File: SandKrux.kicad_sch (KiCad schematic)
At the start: 101 parts, among them CN1 527450697, J1 Conn_01x02, Q1 S8050, Q2 SI2301CDS-T1-GE3, U1 K210_C913414, U2 AXP173, U3 MT9700-N, U4 XC6206P182MR_C347373, U5 GD25LQ128EWIGR, U6 TMI7003C, U7 SGM803-TXN3/TR_C5152602, U8 XC6206P302MR_C347375, X1 X322526MMB4SI

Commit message: TFT CARD
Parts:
- added C51: 10uF, Capacitor_SMD:C_0201_0603Metric, symbol Device:C
- added R28, R29: 10K, Resistor_SMD:R_0201_0603Metric, symbol Device:R
- added U9: HX TF-CARD XG8P H1.5, easyeda2kicad:TF-SMD_HX-TF-CARD-XG8P-H1.5, symbol easyeda2kicad:HXTF-CARDXG8PH1.5
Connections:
- net GND: now also C51.1, U9.10 (GND), U9.11 (GND), U9.12 (GND), U9.6 (VSS2), U9.9 (GND)
- net at C37.1, C4.2, C49.1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: now also C51.2, R28.2, R29.2, U9.4 (VDD)
- new net: R29.1, U9.7 (DAT0)
- new net SPI1_CS_TF: U9.2 (CD/DAT3)
- new net SPI1_MISO: U9.5 (CLK)
- new net SPI1_MOSI: R28.1, U9.3 (CMD)
- no-connect marks 70 -> 72
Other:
- note added: "TF CARD"

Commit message: usb ports
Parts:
- added R30, R31: 5.1K, Resistor_SMD:R_0201_0603Metric, symbol Device:R
- added R32, R33, R34, R35, R36, R37, R38, R39: 1.5K, Resistor_SMD:R_0201_0603Metric, symbol Device:R
- added R40: NC, Resistor_SMD:R_0201_0603Metric, symbol Device:R
- added R41: 0R, Resistor_SMD:R_0201_0603Metric, symbol Device:R
- added SW1, SW2, SW3, SW4, SW5: TL3330AF130QG, easyeda2kicad:SW-SMD_E-SWITCH_TL3330, symbol easyeda2kicad:TL3330AF130QG
- added USB1: HYCW412-USBC16-065B, easyeda2kicad:USB-C-SMD_HYCW412-USBC16-065B, symbol easyeda2kicad:HYCW412-USBC16-065B
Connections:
- net GND: now also R30.1, R31.1, R41.2, SW2.2, SW2.3, SW2.4, SW3.2, SW3.3, SW3.4, SW4.2, SW4.3, SW4.4, SW5.3, SW5.4, USB1.13, USB1.14, USB1.15, USB1.16, USB1.A1B12 (GND), USB1.B1A12 (GND)
- net I2C_SCL: now also R37.2
- net I2C_SDA: now also R36.2
- net RST: now also SW1.1
- net at C37.1, C4.2, C49.1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: now also R32.2, R33.2, R34.2, R35.2, R36.1, R37.1, R38.1, R39.1, R40.2
- new net: R40.1, R41.1, SW5.2
- new net: SW1.3, SW1.4
- new net 5V_USB: USB1.A4B9 (VBUS), USB1.B4A9 (VBUS)
- new net CC1_2: R30.2, USB1.A5 (CC1)
- new net CC2_2: R31.2, USB1.B5 (CC2)
- new net IO17: R34.1
- new net IO19: R35.1
- new net KEY1: R38.2, SW3.1
- new net KEY2: R39.2, SW4.1
- new net KEY3: SW5.1
- new net PWRON: SW2.1
- new net U2RX: R33.1
- new net U2TX: R32.1
- new net USB_D+: USB1.A6 (DP1), USB1.B6 (DP2)
- new net USB_D-: USB1.A7 (DN1), USB1.B7 (DN2)
- no-connect marks 72 -> 74
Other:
- note added: "USB PORTS"

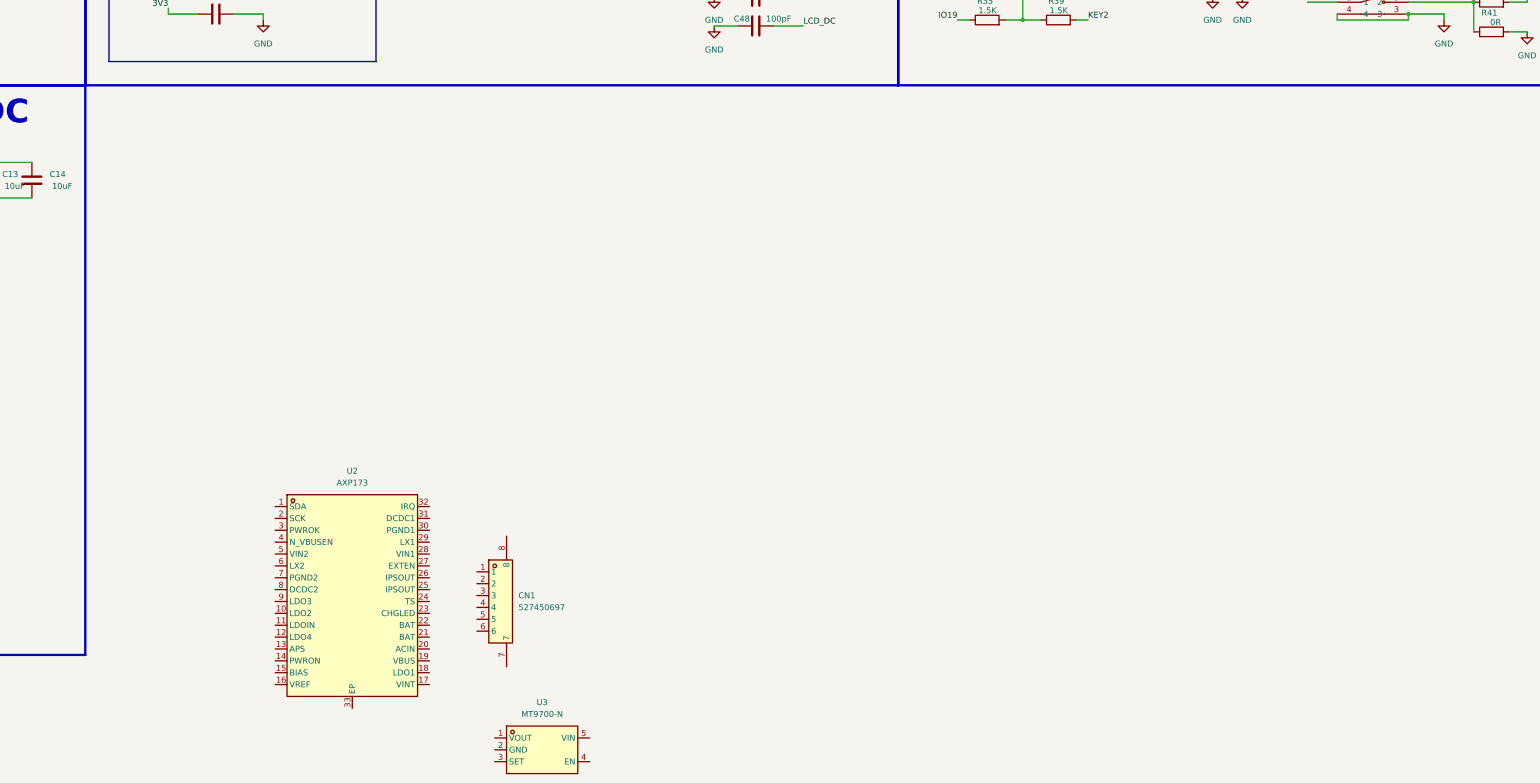
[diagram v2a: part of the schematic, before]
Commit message: AXP173 batery module
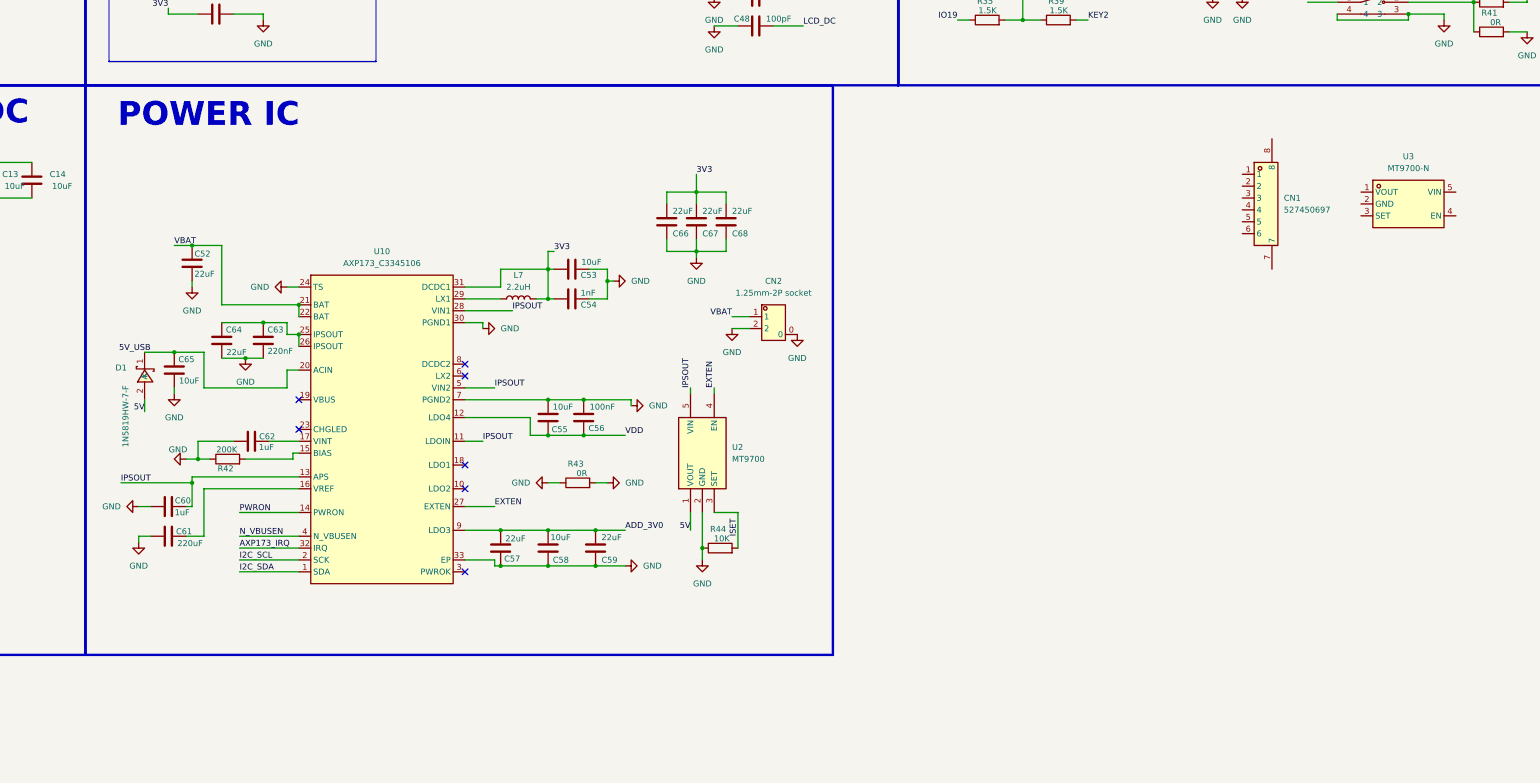
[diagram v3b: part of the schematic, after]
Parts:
- removed U2: AXP173, easyeda2kicad:QFN-32_L5.0-W5.0-P0.50-TL-EP3.5-1, symbol easyeda2kicad:AXP173
- added C52, C57, C59, C64, C66, C67, C68: 22uF, Capacitor_SMD:C_0201_0603Metric, symbol Device:C
- added C53, C55, C58, C65: 10uF, Capacitor_SMD:C_0201_0603Metric, symbol Device:C
- added C54: 1nF, Capacitor_SMD:C_0201_0603Metric, symbol Device:C
- added C56: 100nF, Capacitor_SMD:C_0201_0603Metric, symbol Device:C
- added C60, C62: 1uF, Capacitor_SMD:C_0201_0603Metric, symbol Device:C
- added C61: 220uF, Capacitor_SMD:C_0201_0603Metric, symbol Device:C
- added C63: 220nF, Capacitor_SMD:C_0201_0603Metric, symbol Device:C
- added CN2: 1.25mm-2P socket, easyeda2kicad:CONN-SMD_1.25T-2P, symbol easyeda2kicad:1.25mm-2Psocket
- added D1: 1N5819HW-7-F, easyeda2kicad:SOD-123_L2.7-W1.6-LS3.7-RD, symbol easyeda2kicad:1N5819HW-7-F
- added L7: 2.2uH, symbol Device:L
- added R42: 200K, Resistor_SMD:R_0201_0603Metric, symbol Device:R
- added R43: 0R, Resistor_SMD:R_0201_0603Metric, symbol Device:R
- added R44: 10K, Resistor_SMD:R_0201_0603Metric, symbol Device:R
- added U10: AXP173_C3345106, easyeda2kicad:QFN-32_L5.0-W5.0-P0.50-TL-EP3.5-1, symbol easyeda2kicad:AXP173_C3345106
- added U2: MT9700, easyeda2kicad:SOT-23-5_L3.0-W1.7-P0.95-LS2.8-BR, symbol easyeda2kicad:MT9700
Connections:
- net 5V_USB: now also C65.1, D1.1 (K), U10.20 (ACIN)
- net GND: now also C52.1, C53.1, C54.1, C55.2, C56.2, C57.1, C58.1, C59.1, C60.2, C61.2, C62.2, C63.2, C64.2, C65.2, C66.1, C67.1, C68.1, CN2.0, CN2.2, R42.1, R43.1, R43.2, R44.1, U10.24 (TS), U10.30 (PGND1), U10.33 (EP), U10.7 (PGND2), U2.2 (GND)
- net I2C_SCL: now also U10.2 (SCK)
- net I2C_SDA: now also U10.1 (SDA)
- net PWRON: now also U10.14 (PWRON)
- net at C37.1, C4.2, C49.1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: now also C53.2, C54.2, C66.2, C67.2, C68.2, L7.2, U10.31 (DCDC1)
- new net: R42.2, U10.15 (BIAS)
- new net: C61.1, U10.16 (VREF)
- new net: C62.1, U10.17 (VINT)
- new net: C63.1, C64.1, U10.25 (IPSOUT), U10.26 (IPSOUT)
- new net: L7.1, U10.29 (LX1)
- new net 5V: D1.2 (A), U2.1 (VOUT)
- new net ADD_3V0: C57.2, C58.2, C59.2, U10.9 (LDO3)
- new net AXP173_IRQ: U10.32 (IRQ)
- new net EXTEN: U10.27 (EXTEN), U2.4 (EN)
- new net IPSOUT: C60.1, U10.11 (LDOIN), U10.13 (APS), U10.28 (VIN1), U10.5 (VIN2), U2.5 (VIN)
- new net ISET: R44.2, U2.3 (SET)
- new net N_VBUSEN: U10.4 (N_VBUSEN)
- new net VBAT: C52.2, CN2.1, U10.21 (BAT), U10.22 (BAT)
- new net VDD: C55.1, C56.1, U10.12 (LDO4)
- no-connect marks 74 -> 81
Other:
- note added: "POWER IC"
- moved on the sheet: CN1, U3
